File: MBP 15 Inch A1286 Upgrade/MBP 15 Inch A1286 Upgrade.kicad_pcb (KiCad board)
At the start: 2 copper layers, 0 parts

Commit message: Fixed broken files
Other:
- rule pad_to_mask_clearance: 0.05 -> 0
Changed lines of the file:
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@@
     (uvia_min_size 0.2)
     (uvia_min_drill 0.1)
-    (edge_width 0.05)
+    (edge_width 0.1)
     (segment_width 0.2)
     (pcb_text_width 0.3)
     (pcb_text_size 1.5 1.5)
-    (mod_edge_width 0.12)
+    (mod_edge_width 0.15)
     (mod_text_size 1 1)
     (mod_text_width 0.15)
     (pad_size 1.524 1.524)
     (pad_drill 0.762)
-    (pad_to_mask_clearance 0.05)
+    (pad_to_mask_clearance 0)
     (aux_axis_origin 0 0)
-    (visible_elements 7FFFFFFF)
+    (visible_elements FFFFFF7F)
     (pcbplotparams
       (layerselection 0x010fc_ffffffff)

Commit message: Added 15-inch 1st revision
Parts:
- added J1: 501745-0301, 5017450301, F.Cu at (111.3, 95.4)
- added MH1: MountingHole_2.5mm_Pad, MountingHole:MountingHole_2.5mm_Pad, F.Cu at (125.0, 73.0)
- added P1: , , F.Cu at (110.0, 88.6)
- added REF**: MacBook Air Wireless Card, MBPWirelessUpgrade:MacBook Air Wireless Card, F.Cu at (139.7, 52.7)
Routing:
- net PP3V3_WLAN: track 0.00 -> 23.0 mm
- net PCIE_AP_R2D_N: track 0.00 -> 19.9 mm
- net PCIE_AP_R2D_P: track 0.00 -> 18.5 mm
- net USB_BT_P: track 0.00 -> 18.3 mm
- net PCIE_CLK100M_AP_N: track 0.00 -> 17.8 mm
- net PCIE_AP_D2R_N: track 0.00 -> 16.9 mm
- net USB_BT_N: track 0.00 -> 16.8 mm
- net PCIE_CLK100M_AP_P: track 0.00 -> 16.7 mm
- net PCIE_AP_D2R_P: track 0.00 -> 15.6 mm
- net AP_RESET_CONN_L: track 0.00 -> 14.9 mm, vias 0 -> 2
- net PP3V3_S3_BT_F: track 0.00 -> 14.8 mm, vias 0 -> 2
- net GND: track 0.00 -> 14.4 mm, vias 0 -> 7
- net AP_CLKREQ_Q_L: track 0.00 -> 11.6 mm, vias 0 -> 2
- net AP_PCIE_WAKE_L: track 0.00 -> 10.8 mm, vias 0 -> 2
- net WIFI_EVENT_L: track 0.00 -> 8.93 mm, vias 0 -> 2
- added copper zone on B.Cu, net GND
- added copper zone on F.Cu, net GND
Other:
- board outline added: 27.8 x 29.9 mm
- rule trace_min: 0.2 -> 0.175
- board text added: "Krutav Shah"

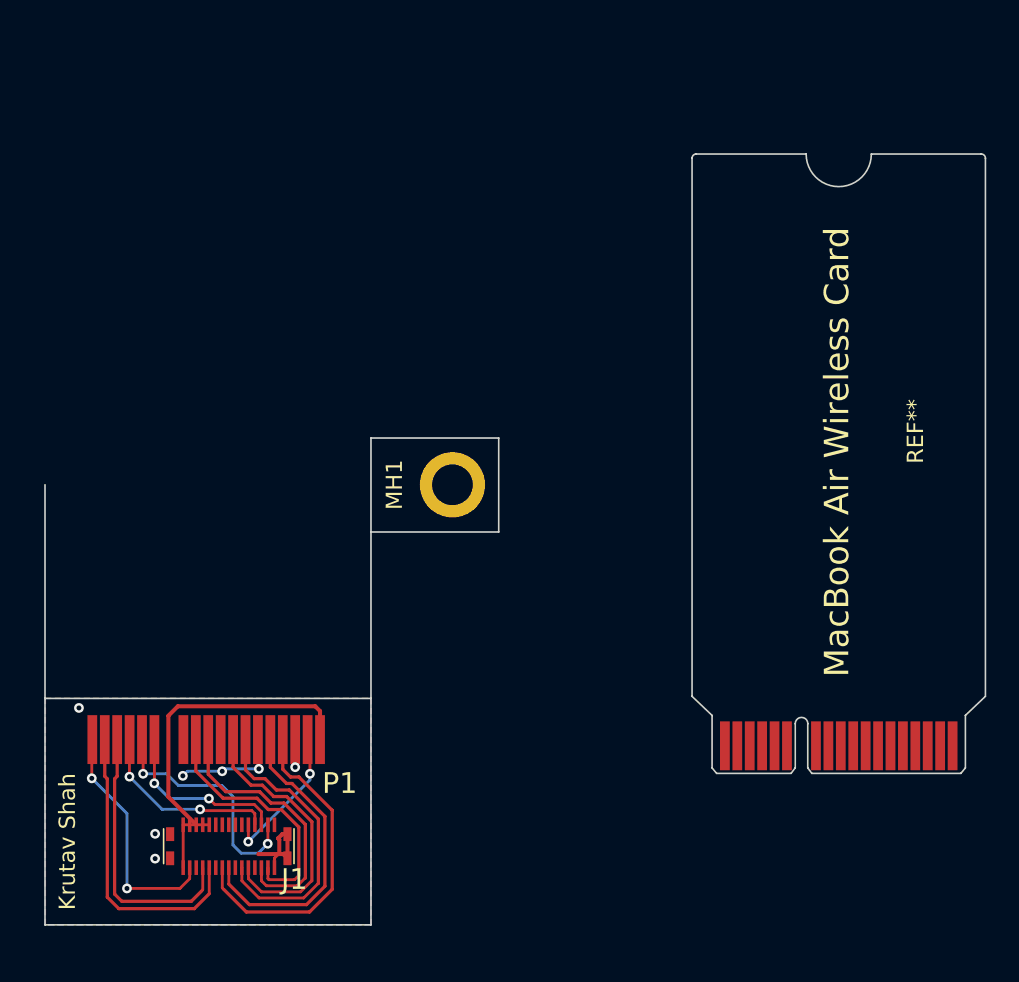
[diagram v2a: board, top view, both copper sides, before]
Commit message: Updated 2009 15-inch adapter
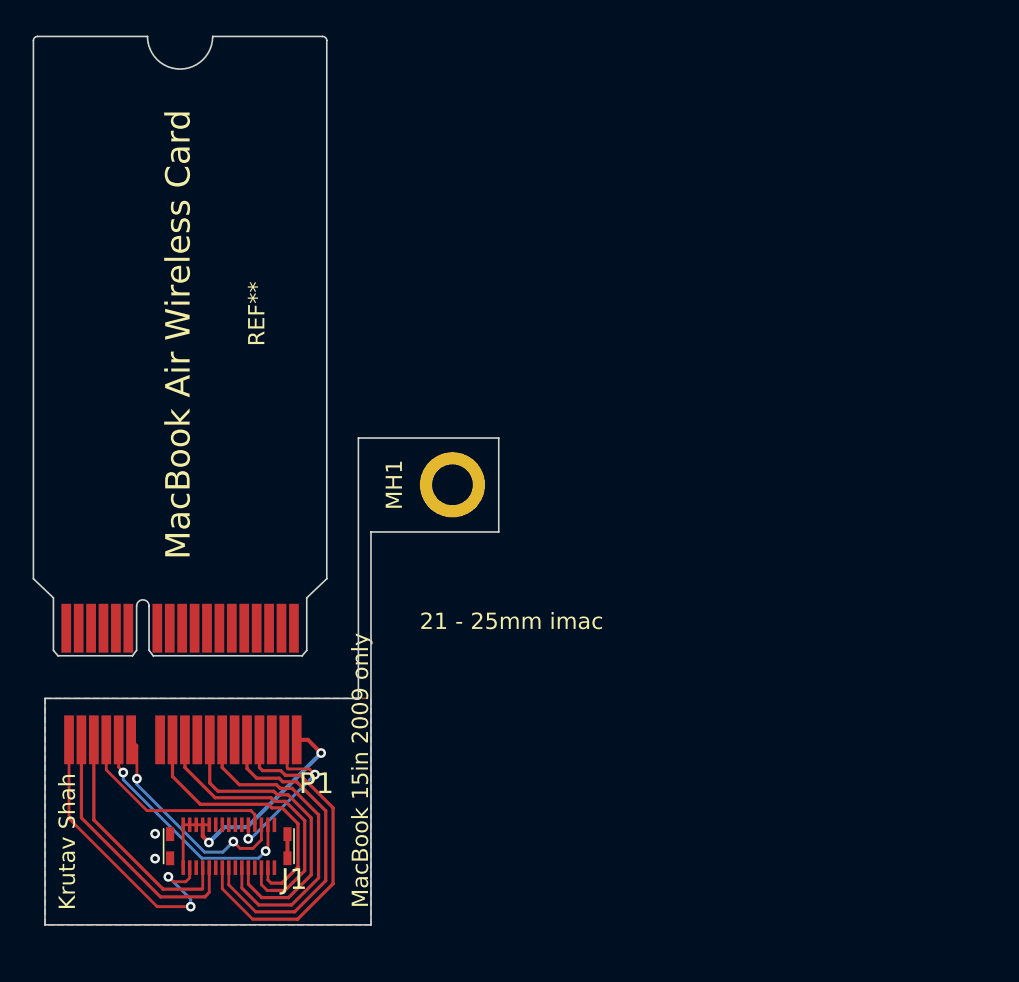
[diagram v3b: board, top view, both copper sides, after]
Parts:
- moved REF** 41.1 mm to (99.3, 45.5)
- moved P1 1.43 mm to (108.6, 88.7)
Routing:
- net GND: track 14.4 -> 1.48 mm, vias 7 -> 2
- net PP3V3_WLAN: track 23.0 -> 16.5 mm, vias 0 -> 2
- net PP3V3_S3_BT_F: track 14.8 -> 19.1 mm
- net AP_PCIE_WAKE_L: track 10.8 -> 13.8 mm
- net PCIE_CLK100M_AP_P: track 16.7 -> 19.1 mm
- net USB_BT_N: track 16.8 -> 14.7 mm
- net USB_BT_P: track 18.3 -> 16.3 mm
- net PCIE_AP_R2D_P: track 18.5 -> 20.4 mm
- net PCIE_CLK100M_AP_N: track 17.8 -> 19.8 mm
- net PCIE_AP_R2D_N: track 19.9 -> 21.7 mm
- net PCIE_AP_D2R_P: track 15.6 -> 17.2 mm
- net WIFI_EVENT_L: track 8.93 -> 10.3 mm
- net AP_CLKREQ_Q_L: track 11.6 -> 12.7 mm, vias 2 -> 0
- net PCIE_AP_D2R_N: track 16.9 -> 17.8 mm
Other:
- outline, holes or cut-outs redrawn
- board text added: "21 - 25mm imac"
- board text added: "MacBook 15in 2009 only"
